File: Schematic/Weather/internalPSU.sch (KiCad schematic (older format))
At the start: 1 part

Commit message: Start PCB
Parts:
- PSU1: footprint (none) -> footprint:PowerBrick
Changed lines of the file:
@@
 F 0 "PSU1" H 3628 1871 50  0000 L CNN
 F 1 "PowerBrick" H 3628 1780 50  0000 L CNN
-F 2 "" H 3200 1550 50  0001 C CNN
+F 2 "footprint:PowerBrick" H 3200 1550 50  0001 C CNN
 F 3 "" H 3200 1550 50  0001 C CNN
 	1    3000 1850

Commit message: more changes
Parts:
- added H1, H2: MountingHole_Pad, Connector_Wire:SolderWirePad_1x01_Drill0.8mm, symbol Mechanical:MountingHole_Pad
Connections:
- net GND: now also H2.1
- net J1_P2: now also H1.1
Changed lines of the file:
@@
 $Descr A4 11693 8268
 encoding utf-8
-Sheet 2 14
+Sheet 2 15
 Title ""
 Date ""
@@
 $EndComp
 Wire Wire Line
-	2000 2000 2500 2000
+	2000 2000 2100 2000
 Wire Wire Line
 	2500 2000 2500 2450
@@
 $EndComp
 Wire Wire Line
-	2000 1750 2900 1750
+	2000 1750 2100 1750
 Wire Wire Line
 	2900 2000 2500 2000
 Connection ~ 2500 2000
+$Comp
+L Mechanical:MountingHole_Pad H?
+U 1 1 5CB5C4AF
+P 2100 1650
+AR Path="/5CAF7F5D/5CB5C4AF" Ref="H?"  Part="1"
+AR Path="/5C9252D8/5CB5C4AF" Ref="H1"  Part="1"
+F 0 "H1" H 2050 1850 50  0000 L CNN
+F 1 "MountingHole_Pad" H 1500 1950 50  0000 L CNN
+F 2 "Connector_Wire:SolderWirePad_1x01_Drill0.8mm" H 2100 1650 50  0001 C CNN
+F 3 "~" H 2100 1650 50  0001 C CNN
+	1    2100 1650
+	1    0    0    -1
+$EndComp
+$Comp
+L Mechanical:MountingHole_Pad H?
+U 1 1 5CB5D5F2
+P 2100 2100
+AR Path="/5CAF7F5D/5CB5D5F2" Ref="H?"  Part="1"
+AR Path="/5C9252D8/5CB5D5F2" Ref="H2"  Part="1"
+F 0 "H2" H 2100 2300 50  0000 L CNN
+F 1 "MountingHole_Pad" H 2050 2400 50  0000 L CNN
+F 2 "Connector_Wire:SolderWirePad_1x01_Drill0.8mm" H 2100 2100 50  0001 C CNN
+F 3 "~" H 2100 2100 50  0001 C CNN
+	1    2100 2100
+	-1   0    0    1
+$EndComp
+Connection ~ 2100 2000
+Wire Wire Line
+	2100 2000 2500 2000
+Connection ~ 2100 1750
+Wire Wire Line
+	2100 1750 2900 1750
 $EndSCHEMATC

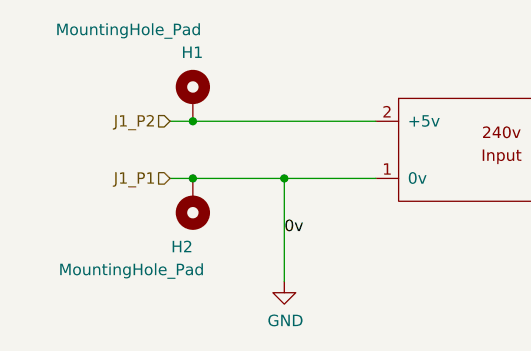
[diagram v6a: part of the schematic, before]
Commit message: Connector relable start
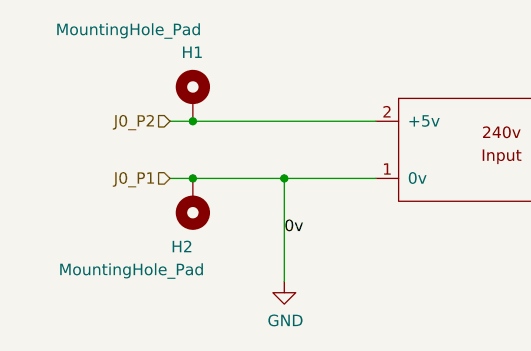
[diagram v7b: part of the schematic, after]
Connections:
- net J1_P2 renamed J0_P2
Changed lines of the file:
@@
 $EndDescr
 Text HLabel 2000 2000 0    50   Input ~ 0
-J1_P1
+J0_P1
 Text HLabel 2000 1750 0    50   Input ~ 0
-J1_P2
+J0_P2
 $Comp
 L power:GND #PWR01

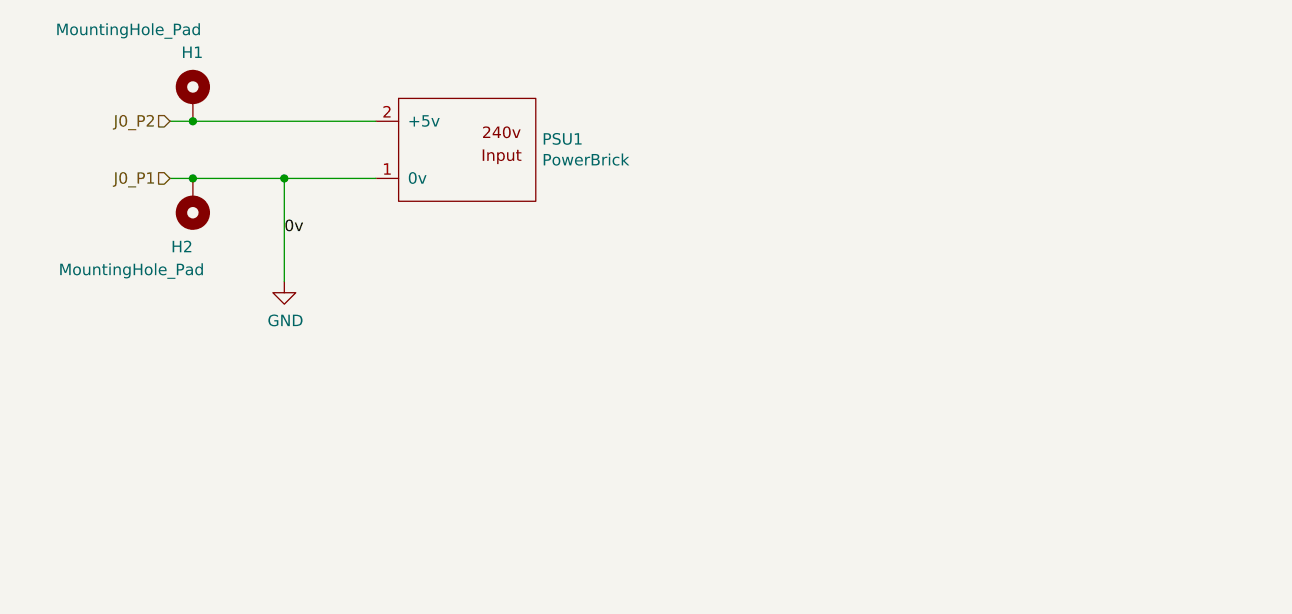
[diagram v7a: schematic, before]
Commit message: Connector changes
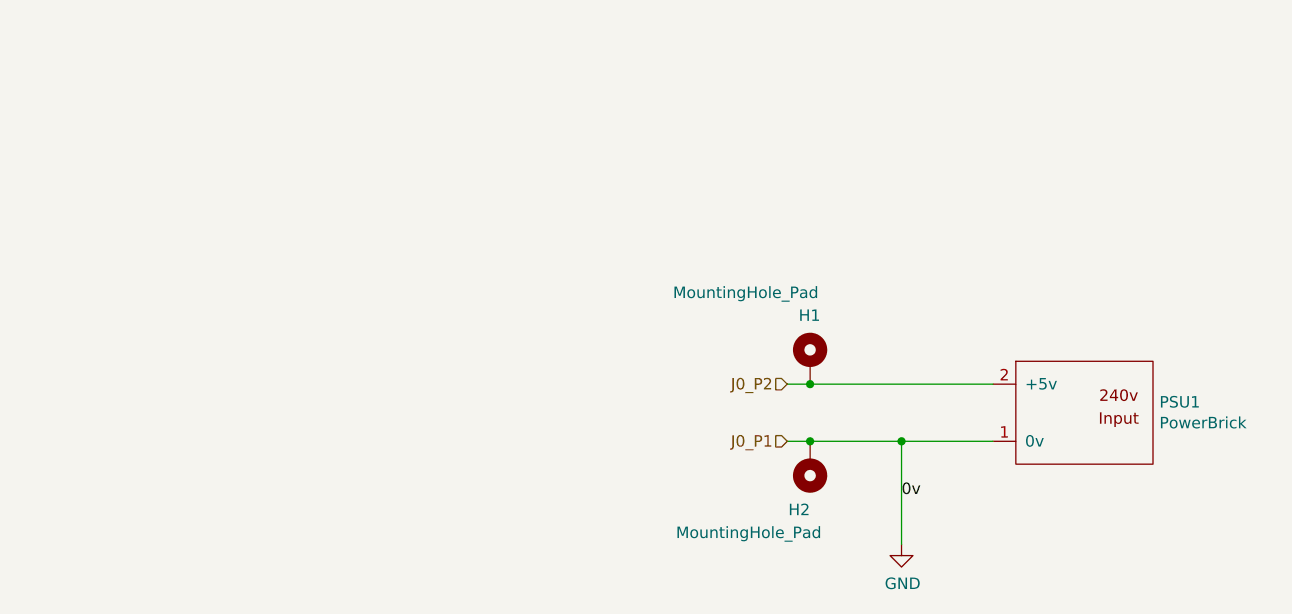
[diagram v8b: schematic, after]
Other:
- moved on the sheet: H1, H2, PSU1
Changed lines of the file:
@@
 Comment4 ""
 $EndDescr
-Text HLabel 2000 2000 0    50   Input ~ 0
+Text HLabel 4700 3150 0    50   Input ~ 0
 J0_P1
-Text HLabel 2000 1750 0    50   Input ~ 0
+Text HLabel 4700 2900 0    50   Input ~ 0
 J0_P2
 $Comp
 L power:GND #PWR01
 U 1 1 5C92A263
-P 2500 2450
-F 0 "#PWR01" H 2500 2200 50  0001 C CNN
-F 1 "GND" H 2505 2277 50  0000 C CNN
-F 2 "" H 2500 2450 50  0001 C CNN
-F 3 "" H 2500 2450 50  0001 C CNN
-	1    2500 2450
+P 5200 3600
+F 0 "#PWR01" H 5200 3350 50  0001 C CNN
+F 1 "GND" H 5205 3427 50  0000 C CNN
+F 2 "" H 5200 3600 50  0001 C CNN
+F 3 "" H 5200 3600 50  0001 C CNN
+	1    5200 3600
 	1    0    0    -1
 $EndComp
 Wire Wire Line
-	2000 2000 2100 2000
+	4700 3150 4800 3150
 Wire Wire Line
-	2500 2000 2500 2450
-Text Label 2500 2250 0    50   ~ 0
+	5200 3150 5200 3600
+Text Label 5200 3400 0    50   ~ 0
 0v
 $Comp
 L MyComponents:PowerBrick PSU1
 U 1 1 5C92F4FB
-P 3000 1850
-F 0 "PSU1" H 3628 1871 50  0000 L CNN
-F 1 "PowerBrick" H 3628 1780 50  0000 L CNN
-F 2 "footprint:PowerBrick" H 3200 1550 50  0001 C CNN
-F 3 "" H 3200 1550 50  0001 C CNN
-	1    3000 1850
+P 5700 3000
+F 0 "PSU1" H 6328 3021 50  0000 L CNN
+F 1 "PowerBrick" H 6328 2930 50  0000 L CNN
+F 2 "footprint:PowerBrick" H 5900 2700 50  0001 C CNN
+F 3 "" H 5900 2700 50  0001 C CNN
+	1    5700 3000
 	1    0    0    -1
 $EndComp
 Wire Wire Line
-	2000 1750 2100 1750
+	4700 2900 4800 2900
 Wire Wire Line
-	2900 2000 2500 2000
-Connection ~ 2500 2000
+	5600 3150 5200 3150
+Connection ~ 5200 3150
 $Comp
 L Mechanical:MountingHole_Pad H?
 U 1 1 5CB5C4AF
-P 2100 1650
+P 4800 2800
 AR Path="/5CAF7F5D/5CB5C4AF" Ref="H?"  Part="1"
 AR Path="/5C9252D8/5CB5C4AF" Ref="H1"  Part="1"
-F 0 "H1" H 2050 1850 50  0000 L CNN
-F 1 "MountingHole_Pad" H 1500 1950 50  0000 L CNN
-F 2 "Connector_Wire:SolderWirePad_1x01_Drill0.8mm" H 2100 1650 50  0001 C CNN
-F 3 "~" H 2100 1650 50  0001 C CNN
-	1    2100 1650
+F 0 "H1" H 4750 3000 50  0000 L CNN
+F 1 "MountingHole_Pad" H 4200 3100 50  0000 L CNN
+F 2 "Connector_Wire:SolderWirePad_1x01_Drill0.8mm" H 4800 2800 50  0001 C CNN
+F 3 "~" H 4800 2800 50  0001 C CNN
+	1    4800 2800
 	1    0    0    -1
 $EndComp
@@
 L Mechanical:MountingHole_Pad H?
 U 1 1 5CB5D5F2
-P 2100 2100
+P 4800 3250
 AR Path="/5CAF7F5D/5CB5D5F2" Ref="H?"  Part="1"
 AR Path="/5C9252D8/5CB5D5F2" Ref="H2"  Part="1"
-F 0 "H2" H 2100 2300 50  0000 L CNN
-F 1 "MountingHole_Pad" H 2050 2400 50  0000 L CNN
-F 2 "Connector_Wire:SolderWirePad_1x01_Drill0.8mm" H 2100 2100 50  0001 C CNN
-F 3 "~" H 2100 2100 50  0001 C CNN
-	1    2100 2100
+F 0 "H2" H 4800 3450 50  0000 L CNN
+F 1 "MountingHole_Pad" H 4750 3550 50  0000 L CNN
+F 2 "Connector_Wire:SolderWirePad_1x01_Drill0.8mm" H 4800 3250 50  0001 C CNN
+F 3 "~" H 4800 3250 50  0001 C CNN
+	1    4800 3250
 	-1   0    0    1
 $EndComp
-Connection ~ 2100 2000
+Connection ~ 4800 3150
 Wire Wire Line
-	2100 2000 2500 2000
-Connection ~ 2100 1750
+	4800 3150 5200 3150
+Connection ~ 4800 2900
 Wire Wire Line
-	2100 1750 2900 1750
+	4800 2900 5600 2900
 $EndSCHEMATC
